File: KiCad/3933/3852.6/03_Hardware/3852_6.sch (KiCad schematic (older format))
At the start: 23 parts, among them CN3 STRIP Prog., P1 SERIAL CONNECTOR, P2 JBAT, P3 TAMPER CONNECTOR, Q1 Q_NMOS_DGS, U2 MSP430G2433IRHN32

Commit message: Kicad and firmware updates
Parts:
- DL1: symbol LED -> LED-RESCUE-3852_6
- P1, P3: Saet_code (none) -> (none)
- Q1: symbol Q_NMOS_DGS -> Q_NMOS_GSD
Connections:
- net TX: now also Q1.2 (S); no longer Q1.3 (S)
- net Yellow: now also Q1.3 (D); no longer Q1.1 (D)
- net at R2.1: now also Q1.1 (G); no longer Q1.2 (G)
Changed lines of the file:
@@
 LIBS:3852_6-rescue
 LIBS:Contatto868-3V-rescue
-LIBS:saet
 LIBS:power
 LIBS:device
@@
 LIBS:contrib
 LIBS:valves
+LIBS:saet
 LIBS:3852_6-cache
 EELAYER 25 0
@@
 encoding utf-8
 Sheet 1 2
-Title "Magnetic Contact 3V on 868.3 MHz - CS 3862"
+Title "Magnetic Contact 3V on 868.3 MHz - CS 3933"
 Date "mercoledì 03 giugno 2015"
 Rev "2.0"
@@
 $EndComp
 $Comp
-L LED DL1
+L LED-RESCUE-3852_6 DL1
 U 1 1 53F31549
 P 8300 2750
@@
 F 2 "Connectors_Molex:Connector_Molex_PicoBlade_53047-0410" H 2350 3750 50  0001 C CNN
 F 3 "" H 2350 3750 50  0000 C CNN
+F 4 " " H 2350 3750 60  0001 C CNN "Saet_code"
 	1    2350 3750
 	-1   0    0    -1
@@
 NoConn ~ 5700 4350
 $Comp
-L Q_NMOS_DGS Q1
+L Q_NMOS_GSD Q1
 U 1 1 5BA24173
 P 3750 4400
@@
 F 2 "Connectors_Molex:Connector_Molex_PicoBlade_53047-0210" H 2550 5700 50  0000 C CNN
 F 3 "" H 2550 5700 50  0000 C CNN
+F 4 " " H 2550 5700 60  0001 C CNN "Saet_code"
 	1    2550 5700
 	-1   0    0    1

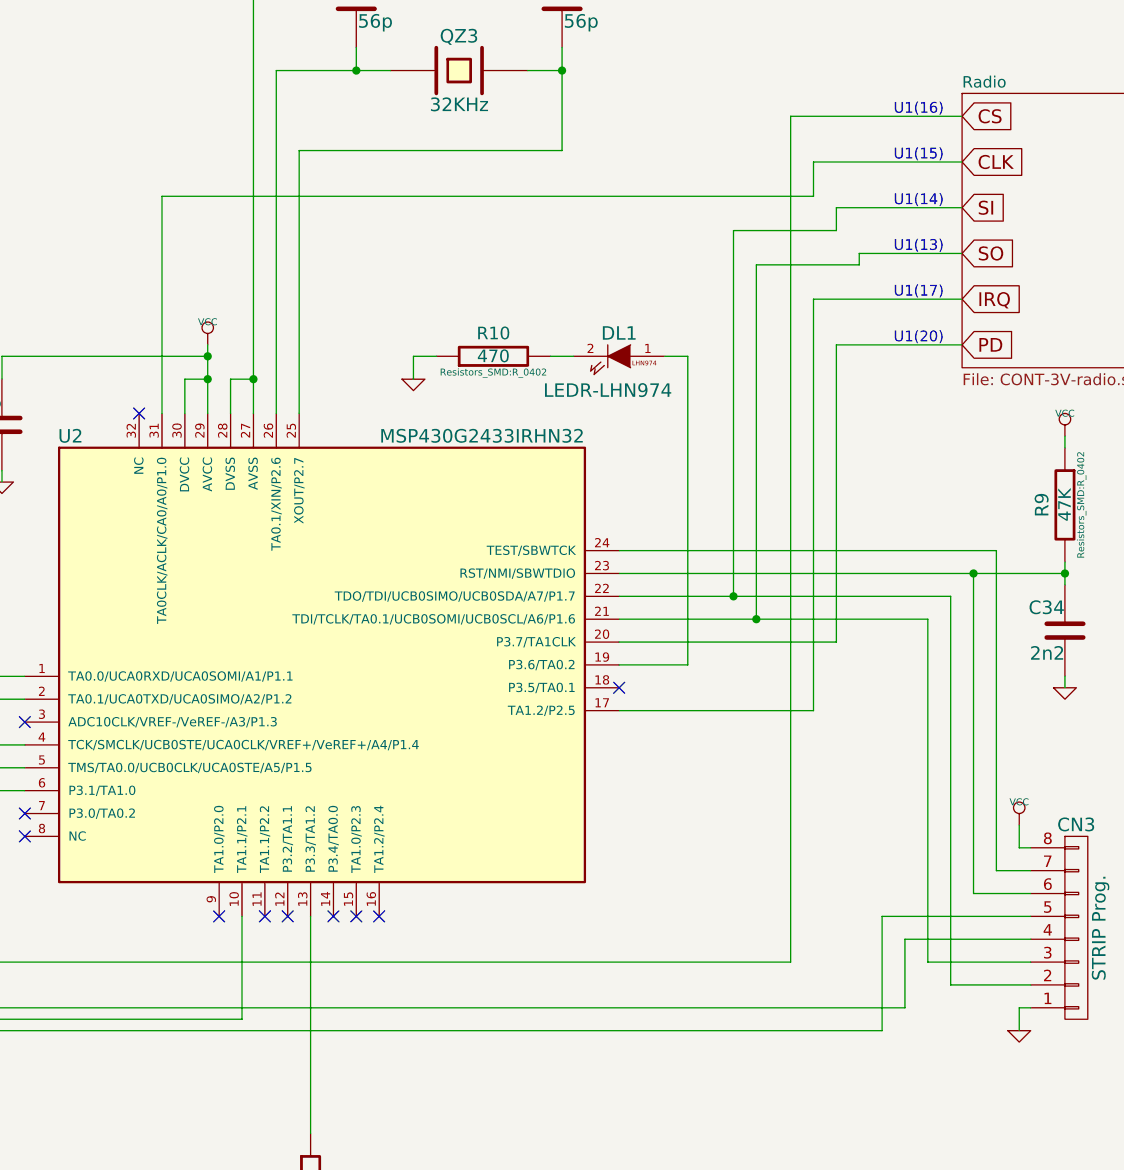
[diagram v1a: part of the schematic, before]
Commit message: Aggiornamenti su modulo SPI (sw->hw) e vari sui circuiti
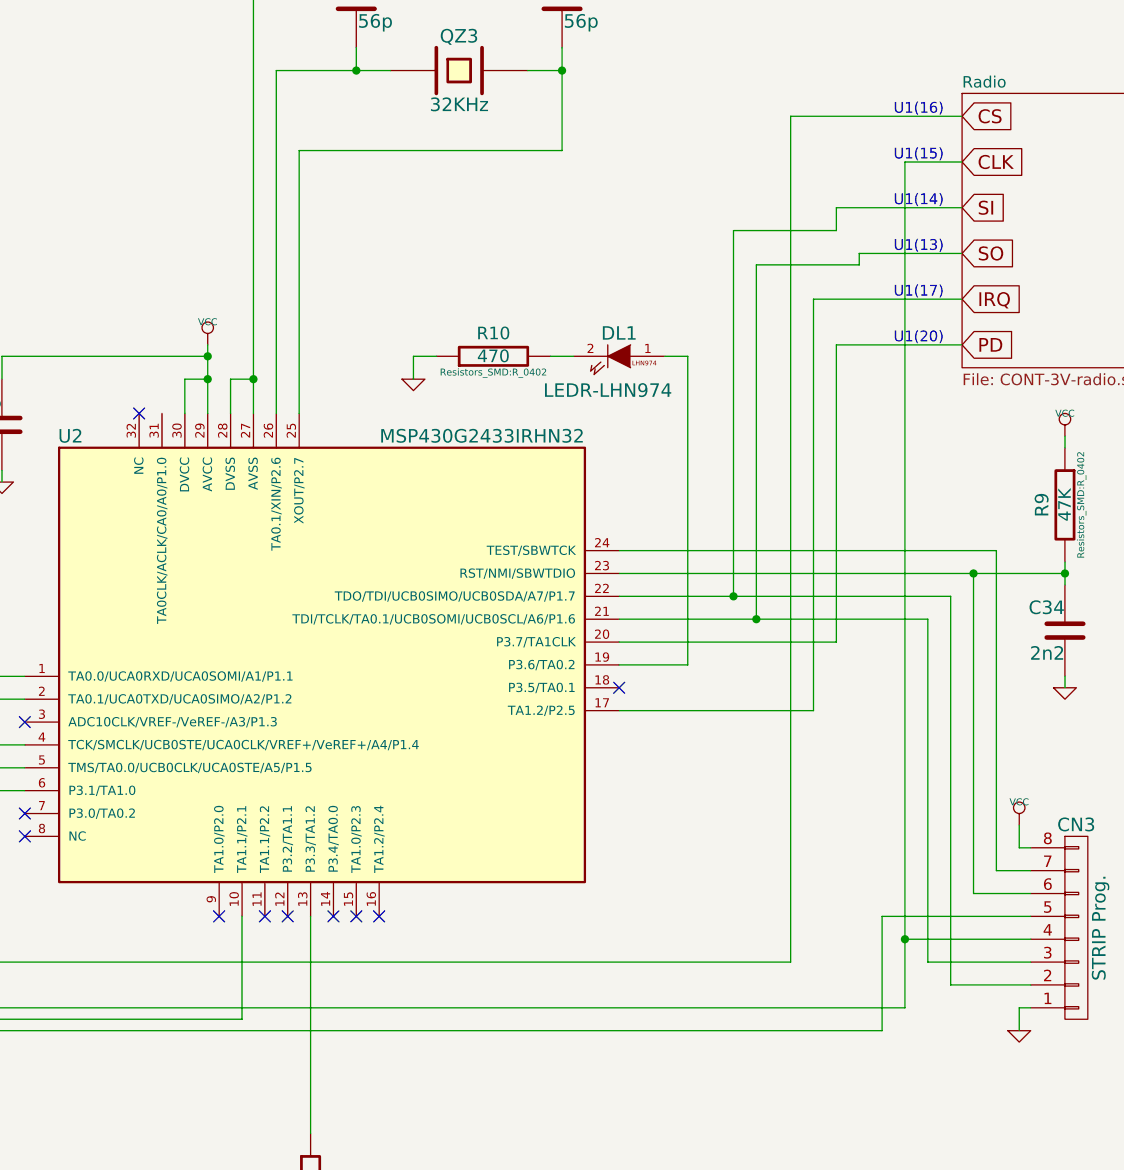
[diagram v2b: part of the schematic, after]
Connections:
- net CLK: now also CN3.4 (P4), U2.5 (TMS/TA0.0/UCB0CLK/UCA0STE/A5/P1.5); no longer U2.31 (TA0CLK/ACLK/CA0/A0/P1.0)
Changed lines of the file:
@@
 	9450 5700 5100 5700
 Wire Wire Line
-	9550 5300 9550 5600
+	9550 1900 9550 5600
 Wire Wire Line
 	9550 5600 5200 5600
@@
 	9800 1700 9050 1700
 Wire Wire Line
-	6300 3000 6300 2050
-Wire Wire Line
 	10100 5600 10050 5600
 Wire Wire Line
@@
 Wire Wire Line
 	8600 2750 8500 2750
-Wire Wire Line
-	9150 2050 9150 1900
-Wire Wire Line
-	9150 1900 9800 1900
 Wire Wire Line
 	9250 2200 9250 2100
@@
 Wire Wire Line
 	7400 2750 7400 2850
-Wire Wire Line
-	6300 2050 9150 2050
 Wire Wire Line
 	8900 2350 8900 3900
@@
 Wire Notes Line
 	750  5350 750  4300
+Wire Wire Line
+	9800 1900 9550 1900
+Connection ~ 9550 5300
 $EndSCHEMATC
